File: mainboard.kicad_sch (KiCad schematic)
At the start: 17 parts, among them J1 Raspi Pi Zero 2W, J10 USBDataBoard, J11 DM, J2 LCD, J3 Keyboard, J4 USB Power, J7 DP, J8 USBDataPi, J9 USB Data, SW1 SW_SPST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

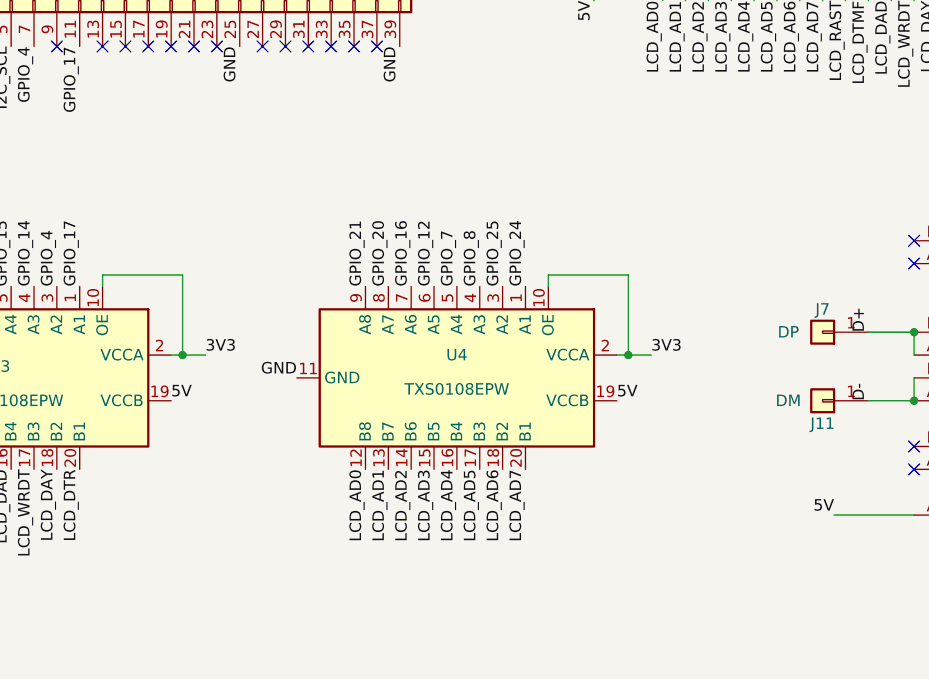
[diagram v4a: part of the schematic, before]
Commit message: adding bypass caps to level shifter
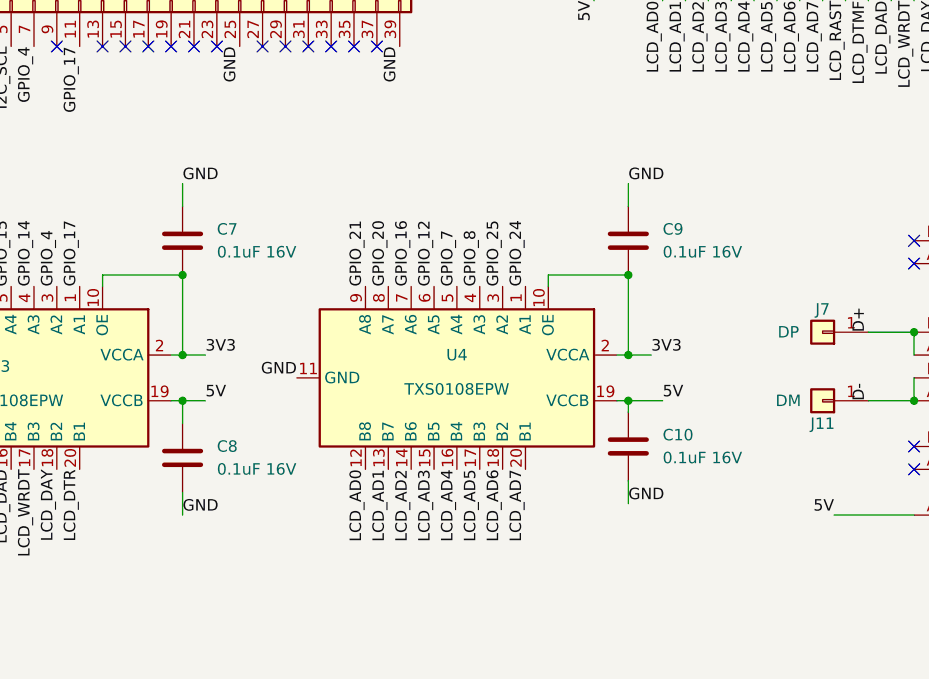
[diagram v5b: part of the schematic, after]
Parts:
- added C10, C7, C8, C9: 0.1uF 16V, Capacitor_SMD:C_0805_2012Metric_Pad1.18x1.45mm_HandSolder, symbol Device:C
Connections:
- net +3V3: now also C7.2, C9.2
- net +5V: now also C10.1, C8.1
- net GND: now also C10.2, C7.1, C8.2, C9.1
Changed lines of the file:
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@@
   (junction (at 254 73.66) (diameter 0) (color 0 0 0 0)
   )
+  (junction (at 222.25 73.66) (diameter 0) (color 0 0 0 0)
+  )
   (junction (at 264.16 25.4) (diameter 0) (color 0 0 0 0)
   )
@@
   (junction (at 102.235 182.88) (diameter 0) (color 0 0 0 0)
   )
+  (junction (at 172.72 59.69) (diameter 0) (color 0 0 0 0)
+  )
   (junction (at 222.25 68.58) (diameter 0) (color 0 0 0 0)
   )
   (junction (at 102.235 190.5) (diameter 0) (color 0 0 0 0)
   )
+  (junction (at 172.72 73.66) (diameter 0) (color 0 0 0 0)
+  )
   (junction (at 53.34 95.25) (diameter 0) (color 0 0 0 0)
   )
@@
   )
   (junction (at 53.34 115.57) (diameter 0) (color 0 0 0 0)
+  )
+  (junction (at 222.25 59.69) (diameter 0) (color 0 0 0 0)
   )
   (junction (at 218.44 25.4) (diameter 0) (color 0 0 0 0)
@@
     (stroke (width 0) (type default) (color 0 0 0 0))
   )
+  (wire (pts (xy 222.25 82.55) (xy 222.25 85.09))
+    (stroke (width 0) (type default) (color 0 0 0 0))
+  )
   (wire (pts (xy 233.68 25.4) (xy 233.68 29.21))
     (stroke (width 0) (type default) (color 0 0 0 0))
@@
     (stroke (width 0) (type default) (color 0 0 0 0))
   )
+  (wire (pts (xy 222.25 73.66) (xy 226.06 73.66))
+    (stroke (width 0) (type default) (color 0 0 0 0))
+  )
   (wire (pts (xy 140.335 144.78) (xy 137.795 144.78))
     (stroke (width 0) (type default) (color 0 0 0 0))
@@
     (stroke (width 0) (type default) (color 0 0 0 0))
   )
+  (wire (pts (xy 171.45 73.66) (xy 172.72 73.66))
+    (stroke (width 0) (type default) (color 0 0 0 0))
+  )
   (wire (pts (xy 59.69 87.63) (xy 63.5 87.63))
     (stroke (width 0) (type default) (color 0 0 0 0))
@@
     (stroke (width 0) (type default) (color 0 0 0 0))
   )
+  (wire (pts (xy 220.98 73.66) (xy 222.25 73.66))
+    (stroke (width 0) (type default) (color 0 0 0 0))
+  )
   (wire (pts (xy 42.545 172.085) (xy 40.005 172.085))
     (stroke (width 0) (type default) (color 0 0 0 0))
@@
     (stroke (width 0) (type default) (color 0 0 0 0))
   )
+  (wire (pts (xy 222.25 49.53) (xy 222.25 52.07))
+    (stroke (width 0) (type default) (color 0 0 0 0))
+  )
   (wire (pts (xy 59.69 67.31) (xy 59.69 77.47))
     (stroke (width 0) (type default) (color 0 0 0 0))
@@
     (stroke (width 0) (type default) (color 0 0 0 0))
   )
+  (wire (pts (xy 172.72 73.66) (xy 172.72 76.2))
+    (stroke (width 0) (type default) (color 0 0 0 0))
+  )
   (wire (pts (xy 226.06 25.4) (xy 226.06 29.21))
     (stroke (width 0) (type default) (color 0 0 0 0))
@@
     (stroke (width 0) (type default) (color 0 0 0 0))
   )
+  (wire (pts (xy 172.72 49.53) (xy 172.72 52.07))
+    (stroke (width 0) (type default) (color 0 0 0 0))
+  )
   (wire (pts (xy 222.25 68.58) (xy 222.25 59.69))
     (stroke (width 0) (type default) (color 0 0 0 0))
@@
     (stroke (width 0) (type default) (color 0 0 0 0))
   )
+  (wire (pts (xy 222.25 73.66) (xy 222.25 74.93))
+    (stroke (width 0) (type default) (color 0 0 0 0))
+  )
   (wire (pts (xy 236.22 25.4) (xy 236.22 29.21))
     (stroke (width 0) (type default) (color 0 0 0 0))
@@
     (stroke (width 0) (type default) (color 0 0 0 0))
   )
+  (wire (pts (xy 172.72 83.82) (xy 172.72 86.36))
+    (stroke (width 0) (type default) (color 0 0 0 0))
+  )
   (wire (pts (xy 259.08 25.4) (xy 259.08 29.21))
     (stroke (width 0) (type default) (color 0 0 0 0))
@@
   )
   (wire (pts (xy 88.9 95.25) (xy 93.98 95.25))
+    (stroke (width 0) (type default) (color 0 0 0 0))
+  )
+  (wire (pts (xy 172.72 73.66) (xy 175.26 73.66))
     (stroke (width 0) (type default) (color 0 0 0 0))
   )
@@
     (effects (font (size 1.27 1.27)) (justify left bottom))
   )
+  (label "GND" (at 172.72 86.36 0)
+    (effects (font (size 1.27 1.27)) (justify left bottom))
+  )
   (label "I2C_SDA" (at 97.79 142.24 180)
     (effects (font (size 1.27 1.27)) (justify right bottom))
@@
     (effects (font (size 1.27 1.27)) (justify right bottom))
   )
-  (label "5V" (at 220.98 73.66 0)
+  (label "5V" (at 226.06 73.66 0)
     (effects (font (size 1.27 1.27)) (justify left bottom))
   )
@@
     (effects (font (size 1.27 1.27)) (justify left bottom))
   )
+  (label "GND" (at 172.72 49.53 0)
+    (effects (font (size 1.27 1.27)) (justify left bottom))
+  )
+  (label "GND" (at 222.25 85.09 0)
+    (effects (font (size 1.27 1.27)) (justify left bottom))
+  )
   (label "3V3" (at 96.52 165.1 180)
     (effects (font (size 1.27 1.27)) (justify right bottom))
@@
     (effects (font (size 1.27 1.27)) (justify right bottom))
   )
-  (label "5V" (at 171.45 73.66 0)
+  (label "5V" (at 175.26 73.66 0)
     (effects (font (size 1.27 1.27)) (justify left bottom))
   )
   (label "LCD_DTR" (at 259.08 29.21 270)
     (effects (font (size 1.27 1.27)) (justify right bottom))
+  )
+  (label "GND" (at 222.25 49.53 0)
+    (effects (font (size 1.27 1.27)) (justify left bottom))
   )
   (label "KB7" (at 140.335 180.34 0)
@@
     (pin "1")
   )
+  (symbol (lib_id "Device:C") (at 222.25 78.74 0) (unit 1)
+    (in_bom yes) (on_board yes) (fields_autoplaced)
+    (property "Reference" "C10" (id 0) (at 226.06 77.4699 0)
+      (effects (font (size 1.27 1.27)) (justify left))
+    )
+    (property "Value" " 0.1uF 16V" (id 1) (at 226.06 80.0099 0)
+      (effects (font (size 1.27 1.27)) (justify left))
+    )
+    (property "Footprint" "Capacitor_SMD:C_0805_2012Metric_Pad1.18x1.45mm_HandSolder" (id 2) (at 223.2152 82.55 0)
+      (effects (font (size 1.27 1.27)) hide)
+    )
+    (property "Datasheet" "~" (id 3) (at 222.25 78.74 0)
+      (effects (font (size 1.27 1.27)) hide)
+    )
+    (pin "1")
+    (pin "2")
+  )
+  (symbol (lib_id "Device:C") (at 222.25 55.88 0) (unit 1)
+    (in_bom yes) (on_board yes) (fields_autoplaced)
+    (property "Reference" "C9" (id 0) (at 226.06 54.6099 0)
+      (effects (font (size 1.27 1.27)) (justify left))
+    )
+    (property "Value" " 0.1uF 16V" (id 1) (at 226.06 57.1499 0)
+      (effects (font (size 1.27 1.27)) (justify left))
+    )
+    (property "Footprint" "Capacitor_SMD:C_0805_2012Metric_Pad1.18x1.45mm_HandSolder" (id 2) (at 223.2152 59.69 0)
+      (effects (font (size 1.27 1.27)) hide)
+    )
+    (property "Datasheet" "~" (id 3) (at 222.25 55.88 0)
+      (effects (font (size 1.27 1.27)) hide)
+    )
+    (pin "1")
+    (pin "2")
+  )
   (symbol (lib_id "Connector_Generic:Conn_01x01") (at 243.84 73.66 180) (unit 1)
     (in_bom yes) (on_board yes)
@@
     (pin "8")
     (pin "9")
+  )
+  (symbol (lib_id "Device:C") (at 172.72 80.01 0) (unit 1)
+    (in_bom yes) (on_board yes) (fields_autoplaced)
+    (property "Reference" "C8" (id 0) (at 176.53 78.7399 0)
+      (effects (font (size 1.27 1.27)) (justify left))
+    )
+    (property "Value" " 0.1uF 16V" (id 1) (at 176.53 81.2799 0)
+      (effects (font (size 1.27 1.27)) (justify left))
+    )
+    (property "Footprint" "Capacitor_SMD:C_0805_2012Metric_Pad1.18x1.45mm_HandSolder" (id 2) (at 173.6852 83.82 0)
+      (effects (font (size 1.27 1.27)) hide)
+    )
+    (property "Datasheet" "~" (id 3) (at 172.72 80.01 0)
+      (effects (font (size 1.27 1.27)) hide)
+    )
+    (pin "1")
+    (pin "2")
   )
   (symbol (lib_id "Connector_Generic:Conn_01x02") (at 261.62 101.6 0) (mirror y) (unit 1)
@@
     (pin "2")
   )
+  (symbol (lib_id "Device:C") (at 172.72 55.88 0) (unit 1)
+    (in_bom yes) (on_board yes) (fields_autoplaced)
+    (property "Reference" "C7" (id 0) (at 176.53 54.6099 0)
+      (effects (font (size 1.27 1.27)) (justify left))
+    )
+    (property "Value" " 0.1uF 16V" (id 1) (at 176.53 57.1499 0)
+      (effects (font (size 1.27 1.27)) (justify left))
+    )
+    (property "Footprint" "Capacitor_SMD:C_0805_2012Metric_Pad1.18x1.45mm_HandSolder" (id 2) (at 173.6852 59.69 0)
+      (effects (font (size 1.27 1.27)) hide)
+    )
+    (property "Datasheet" "~" (id 3) (at 172.72 55.88 0)
+      (effects (font (size 1.27 1.27)) hide)
+    )
+    (pin "1")
+    (pin "2")
+  )
   (sheet (at 234.95 147.955) (size 45.085 11.43) (fields_autoplaced)
     (stroke (width 0.1524) (type solid) (color 0 0 0 0))
@@
       (reference "C6") (unit 1) (value "22u 10V") (footprint "Capacitor_SMD:C_0805_2012Metric_Pad1.18x1.45mm_HandSolder")
     )
+    (path "/f9af1e8f-764c-4c65-a7ab-85f53479cef5"
+      (reference "C7") (unit 1) (value " 0.1uF 16V") (footprint "Capacitor_SMD:C_0805_2012Metric_Pad1.18x1.45mm_HandSolder")
+    )
+    (path "/7552c0d8-0ee6-49ed-9c73-b004d72b03c6"
+      (reference "C8") (unit 1) (value " 0.1uF 16V") (footprint "Capacitor_SMD:C_0805_2012Metric_Pad1.18x1.45mm_HandSolder")
+    )
+    (path "/3bc69df3-eddc-4b1f-aa67-09b076e8eb60"
+      (reference "C9") (unit 1) (value " 0.1uF 16V") (footprint "Capacitor_SMD:C_0805_2012Metric_Pad1.18x1.45mm_HandSolder")
+    )
+    (path "/33884c4e-dad3-4dde-8110-4467ffdcba22"
+      (reference "C10") (unit 1) (value " 0.1uF 16V") (footprint "Capacitor_SMD:C_0805_2012Metric_Pad1.18x1.45mm_HandSolder")
+    )
     (path "/00000000-0000-0000-0000-00006261f0a8"
